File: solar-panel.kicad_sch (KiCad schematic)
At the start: 33 parts

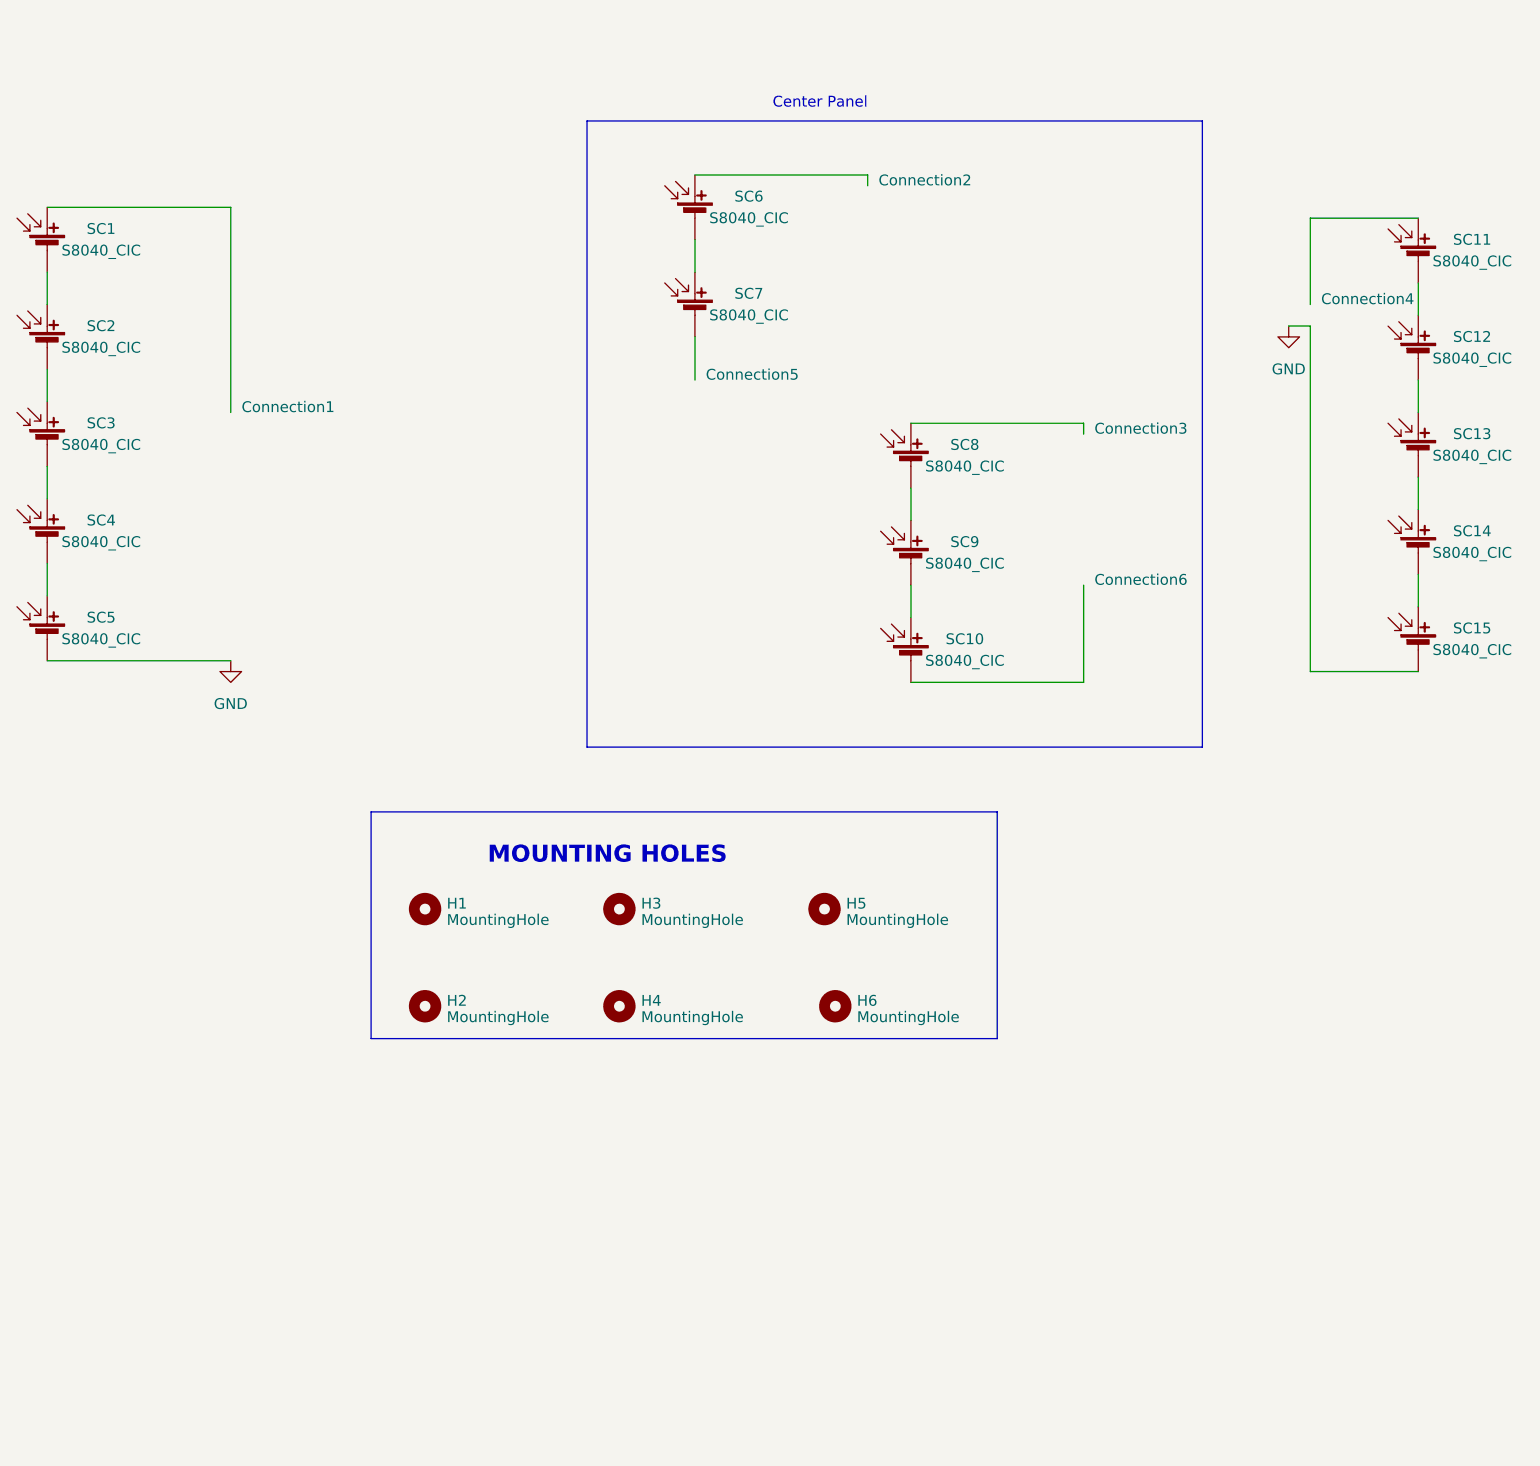
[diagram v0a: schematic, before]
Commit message: Replace solder pads with hirose df13 connections
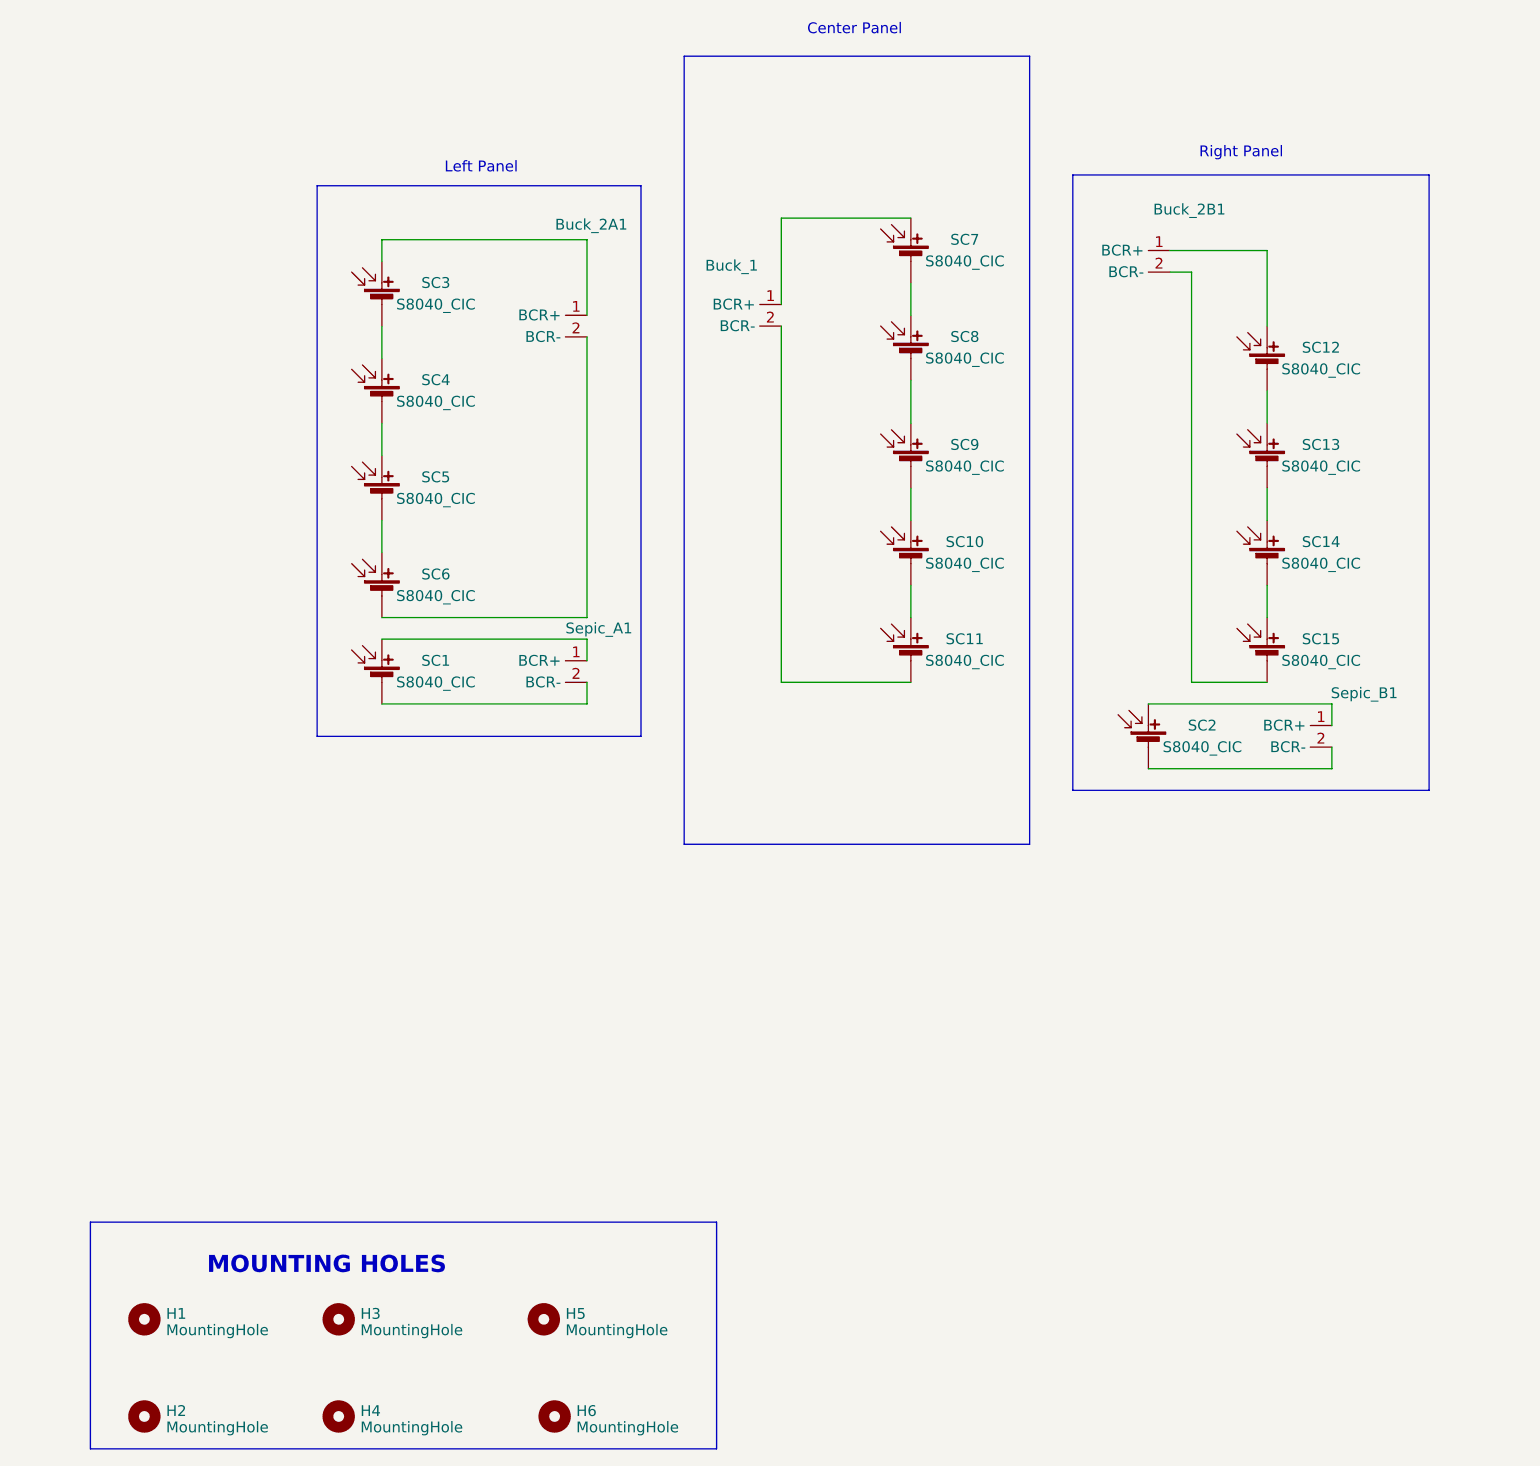
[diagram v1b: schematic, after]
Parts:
- removed Connection2, Connection3, Connection4: ~, symbol Connection_Pads:Series_Connection
- removed Connection6: ~, Connection_Pads:Series_Connection_Pad, symbol Connection_Pads:Series_Connection
- removed Solder_Pad4, Solder_Pad5, Solder_Pad6: ~, Connection_Pads:Series_Connection_Pad, symbol Connection_Pads:Pad
- added Buck_1, Buck_2A1, Buck_2B1, Sepic_A1, Sepic_B1: ~, Connection_Pads:2_Hirose_Pin, symbol Connection_Pads:Pout_Hirose
- added Hirose_Connector1, Hirose_Connector2, Hirose_Connector3: ~, Connector_Hirose:Hirose_DF13-05P-1.25DSA_1x05_P1.25mm_Vertical, symbol Connection_Pads:Hirose_Connector
- renumbered Connection5 to Connection2, SC9 to SC10, SC10 to SC11, SC11 to SC2, SC2 to SC3, SC3 to SC4, SC4 to SC5, SC5 to SC6, SC6 to SC7, SC7 to SC8, SC8 to SC9
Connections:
- net at SC2.1 (+): now also Sepic_B1.1 (BCR+)
- net at SC2.2 (-): now also Sepic_B1.2 (BCR-); no longer SC12.1 (+)
- net at SC9.1 (+): now also SC8.2 (-)
- net at SC1.2 (-): now also Sepic_A1.2 (BCR-); no longer SC3.1 (+)
- net at SC7.1 (+): now also Buck_1.1 (BCR+)
- net at SC1.1 (+): now also Sepic_A1.1 (BCR+)
- net at SC11.2 (-): now also Buck_1.2 (BCR-)
- net GND: no longer names the net of SC6.2 (-)
- net GND: now also Buck_2A1.2 (BCR-); no longer SC15.2 (-)
- new net: Buck_2B1.2 (BCR-), SC15.2 (-)
- new net: Buck_2A1.1 (BCR+), SC3.1 (+)
- new net: Buck_2B1.1 (BCR+), SC12.1 (+)
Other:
- note added: "Left Panel"
- note added: "Right Panel"
- moved on the sheet: H1, H2, H3, H4, H5, H6, SC1, SC12, SC13, SC14, SC15, SC2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

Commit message: Added Mounting holes, overlapped cells, changed to 5 6 3 configuration, changed overall solar panel dimensions
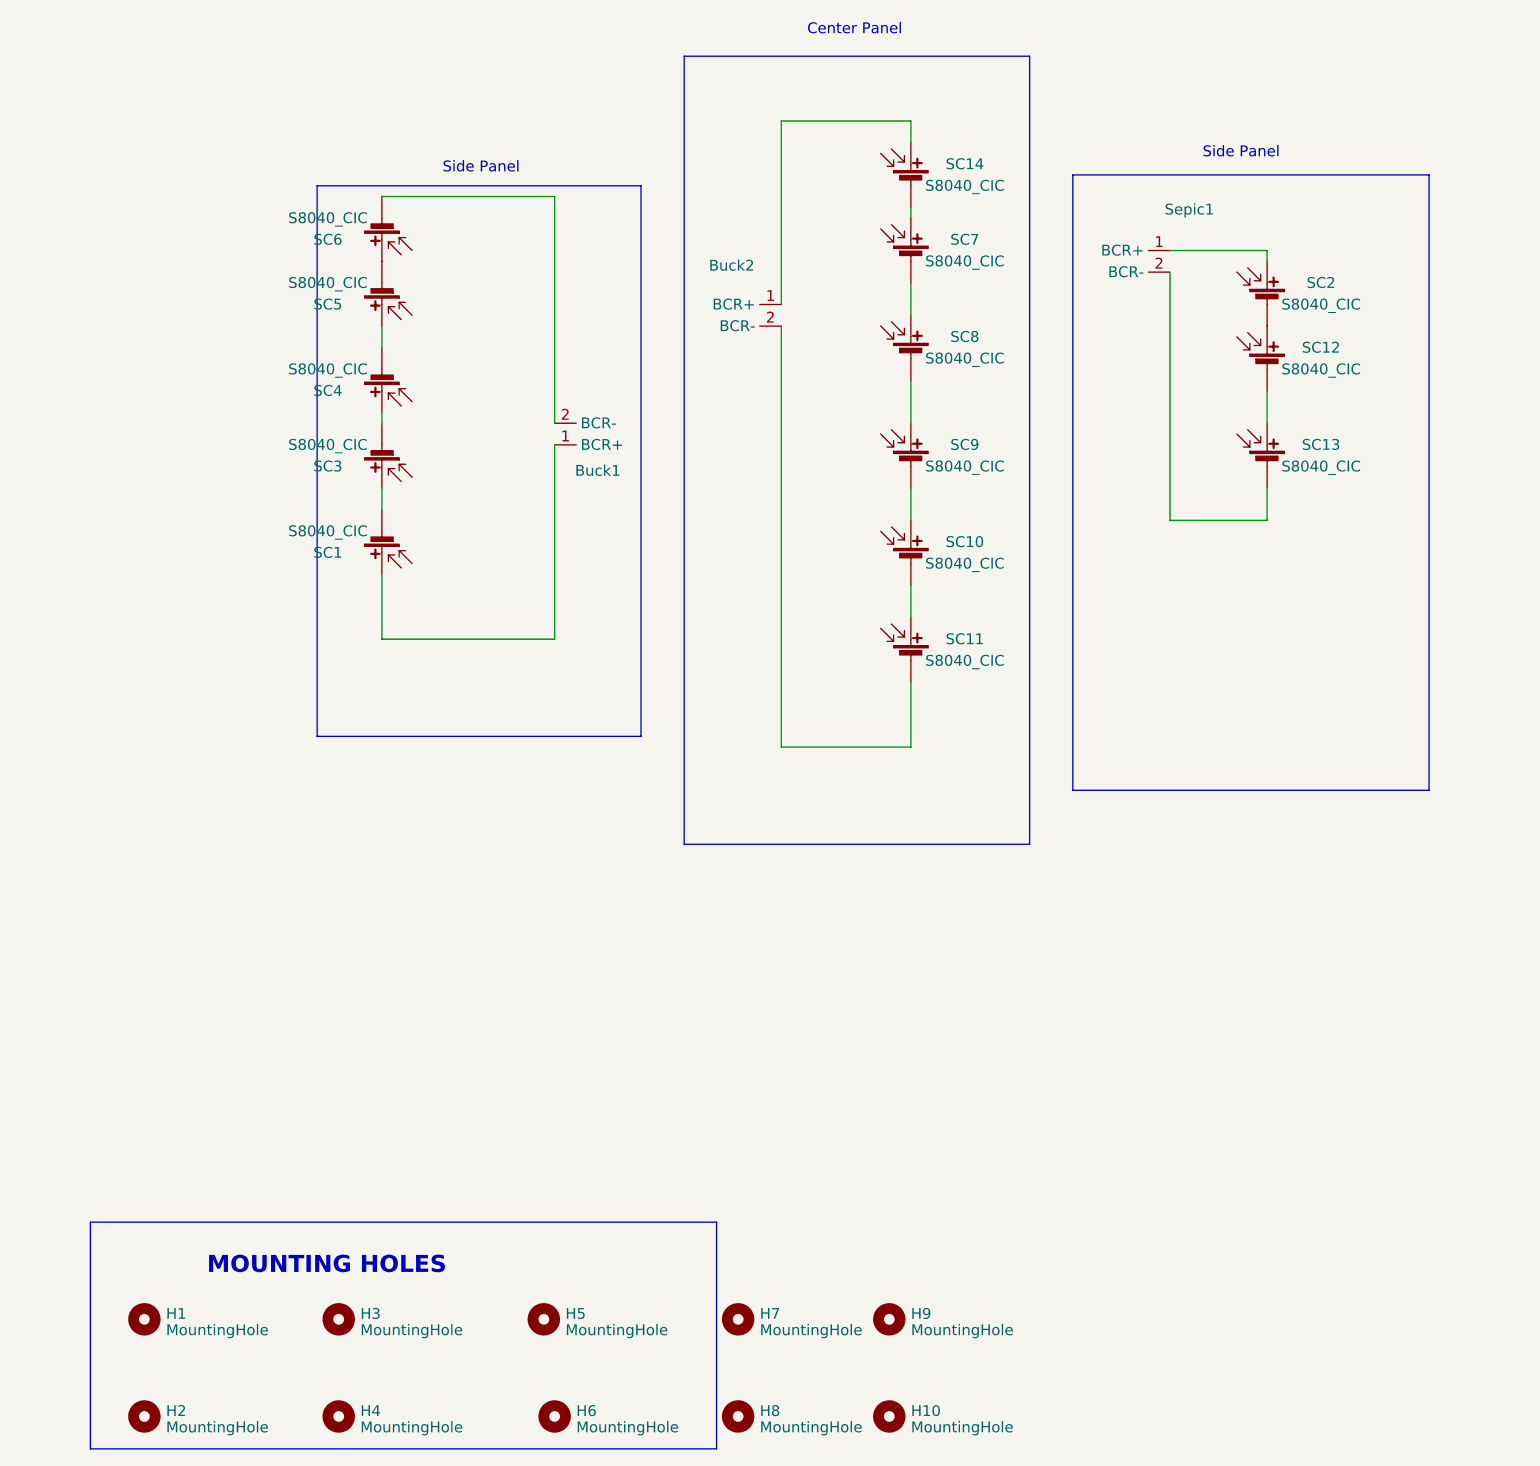
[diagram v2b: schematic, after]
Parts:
- removed SC15: S8040_CIC, Solar_cell:Solar_Cell_Lightricity_S8040_CIC, symbol Device:Solar_Cell
- removed Sepic_A1, Sepic_B1: ~, Connection_Pads:2_Hirose_Pin, symbol Connection_Pads:Pout_Hirose
- added H10, H7, H8, H9: MountingHole, MountingHole:MountingHole_2.7mm, symbol Mechanical:MountingHole
- renumbered Buck_2A1 to Buck1, Buck_1 to Buck2, Buck_2B1 to Sepic1
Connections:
- net at SC1.1 (+): now also Buck1.1 (BCR+)
- net at SC1.2 (-): now also SC3.1 (+)
- net at SC2.1 (+): now also Sepic1.1 (BCR+)
- net at SC2.2 (-): now also SC12.1 (+)
- net at SC13.2 (-): now also Sepic1.2 (BCR-); no longer SC14.1 (+)
- net at SC14.2 (-): now also SC7.1 (+)
- net at Buck2.1 (BCR+): now also SC14.1 (+); no longer SC7.1 (+)
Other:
- note added: "Side Panel"
- note removed: "Left Panel"
- note removed: "Right Panel"
- moved on the sheet: Buck1, SC1, SC14, SC2, SC3, SC4, SC5, SC6
